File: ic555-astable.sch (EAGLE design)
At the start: 9 parts, among them IC1 NE555N

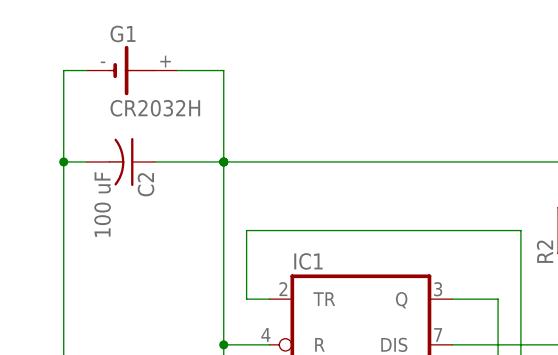
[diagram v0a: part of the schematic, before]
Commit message: Fix board and schematic inconsistency
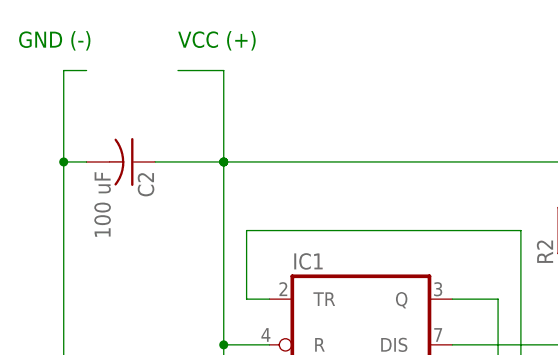
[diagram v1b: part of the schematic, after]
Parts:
- removed G1: CR2032H, battery:CR2032H
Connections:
- net N$4: no longer G1.-
- net N$7: no longer G1.+
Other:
- note added: "GND (-)"
- note added: "VCC (+)"
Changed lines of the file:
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@@
 <part name="C3" library="resistor" deviceset="C-EU" device="050-035X075" value="100 nF"/>
 <part name="LED1" library="led" deviceset="LED" device="5MM"/>
-<part name="G1" library="battery" deviceset="CR2032H" device=""/>
 <part name="R1" library="resistor" deviceset="R-EU_" device="0204/7" value="1k"/>
 <part name="R2" library="resistor" deviceset="R-EU_" device="0204/7" value="1k"/>
@@
 <sheet>
 <plain>
+<text x="33.02" y="91.44" size="1.778" layer="91">VCC (+)</text>
+<text x="15.24" y="91.44" size="1.778" layer="91">GND (-)</text>
 </plain>
 <instances>
@@
 <instance part="C3" gate="G$1" x="27.94" y="53.34" rot="R270"/>
 <instance part="LED1" gate="G$1" x="60.96" y="33.02" rot="R270"/>
-<instance part="G1" gate="1" x="27.94" y="88.9"/>
 <instance part="R1" gate="G$1" x="48.26" y="33.02"/>
 <instance part="R2" gate="G$1" x="76.2" y="71.12" rot="R90"/>
@@
 <wire x1="30.48" y1="78.74" x2="38.1" y2="78.74" width="0.1524" layer="91"/>
 <wire x1="38.1" y1="78.74" x2="38.1" y2="88.9" width="0.1524" layer="91"/>
-<pinref part="G1" gate="1" pin="+"/>
 <wire x1="38.1" y1="88.9" x2="33.02" y2="88.9" width="0.1524" layer="91"/>
 <junction x="38.1" y="78.74"/>
@@
 <wire x1="43.18" y1="33.02" x2="20.32" y2="33.02" width="0.1524" layer="91"/>
 <wire x1="20.32" y1="33.02" x2="20.32" y2="48.26" width="0.1524" layer="91"/>
-<pinref part="G1" gate="1" pin="-"/>
 <wire x1="20.32" y1="48.26" x2="20.32" y2="53.34" width="0.1524" layer="91"/>
 <wire x1="20.32" y1="53.34" x2="20.32" y2="78.74" width="0.1524" layer="91"/>
